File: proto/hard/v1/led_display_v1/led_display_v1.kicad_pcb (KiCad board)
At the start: 2 copper layers, 87 x 50 mm, 100 parts, among them U1 LCD_2.8_SPI, U2 74HCT595, U3 74HCT595, U4 74HCT595

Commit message: Generated gerbers for LED indicator.
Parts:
- moved REF** 0.76 mm to (109.4, 82.5)

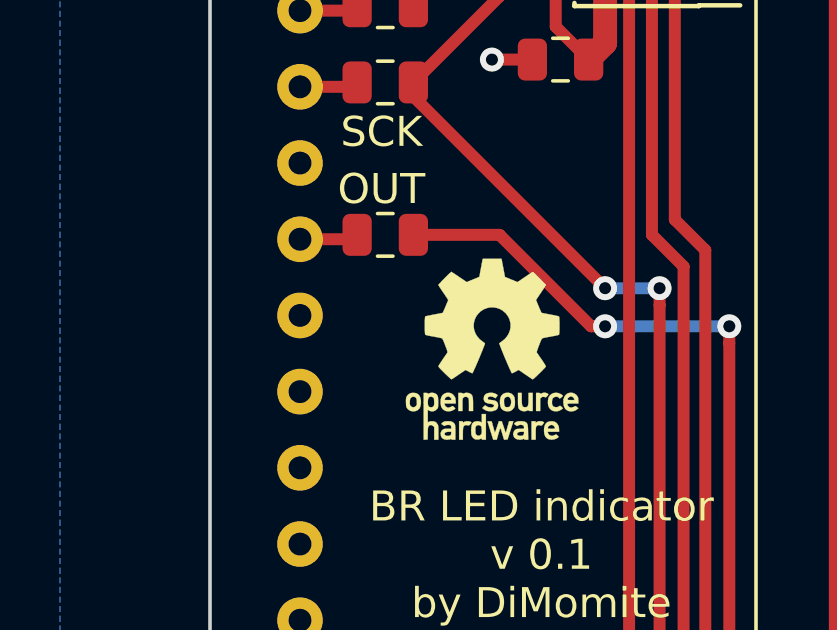
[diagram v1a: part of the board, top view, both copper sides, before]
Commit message: Added voltage divider to LED display data output. Module powered by +5V, so we may need divider to work with +3.3V components.
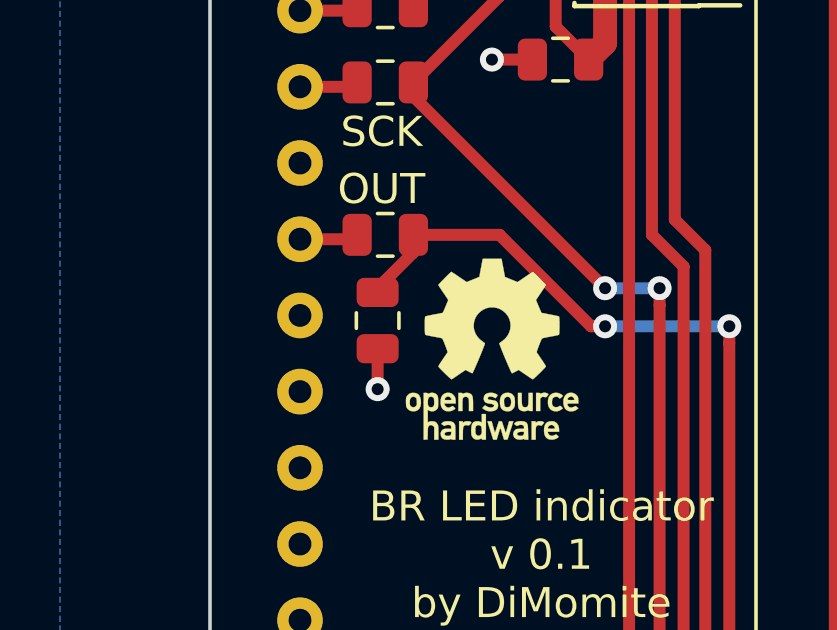
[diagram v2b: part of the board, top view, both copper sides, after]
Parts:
- added R38: 100R, Resistor_SMD:R_0805_2012Metric, F.Cu at (105.6, 81.5)
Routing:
- net /DataOut: track 64.1 -> 66.5 mm
- net GND: track 51.0 -> 52.3 mm, vias 38 -> 39

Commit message: Started implementation of LED display ctrl. Fixed wrong segments naming on led_display board.
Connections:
- R13 pad 2: /N2_E -> /N2_F
- R14 pad 2: /N2_F -> /N2_E
- R6 pad 2: /N1_E -> /N1_F
- R7 pad 2: /N1_F -> /N1_E
- U3 pad 6: /N1_F -> /N1_E
- U3 pad 7: /N1_E -> /N1_F
- U4 pad 6: /N2_F -> /N2_E
- U4 pad 7: /N2_E -> /N2_F

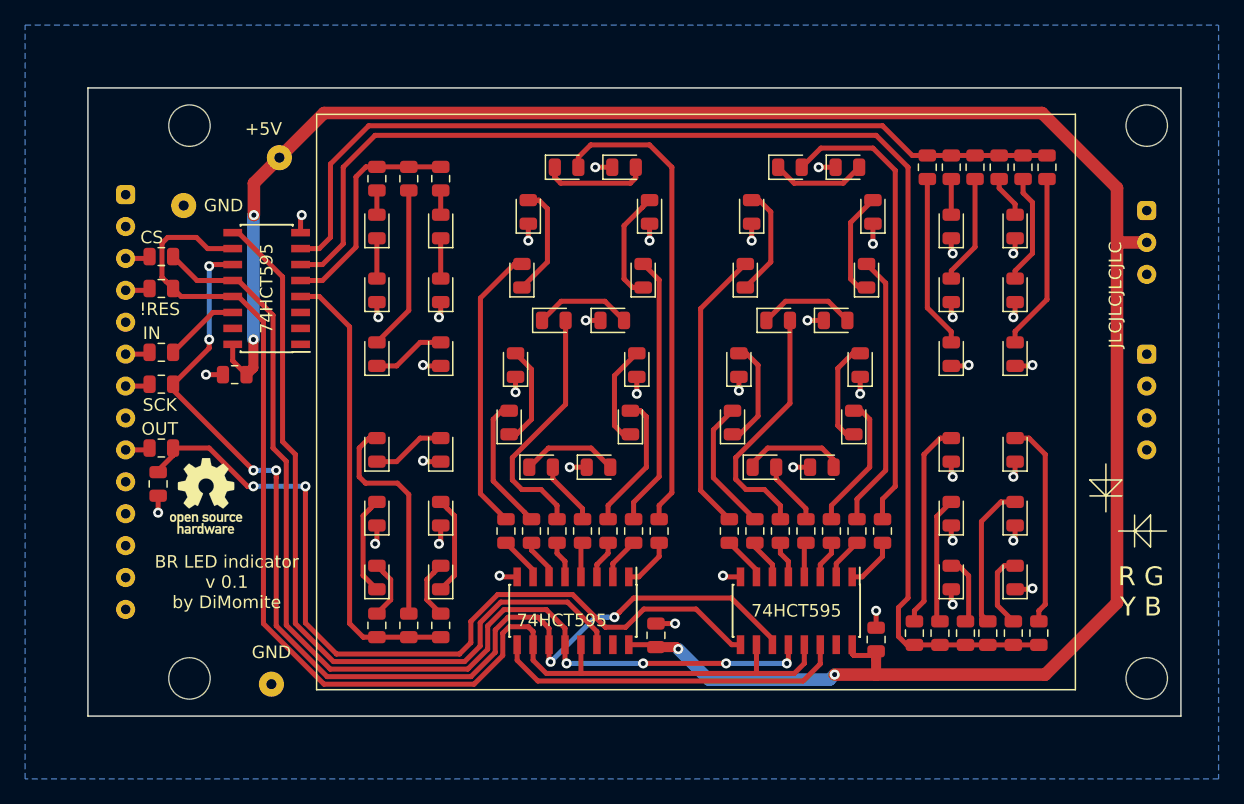
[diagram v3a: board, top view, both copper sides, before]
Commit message: Change SRCLR pin connection to external resistor pulled to +5. Board version increment to 0.2.
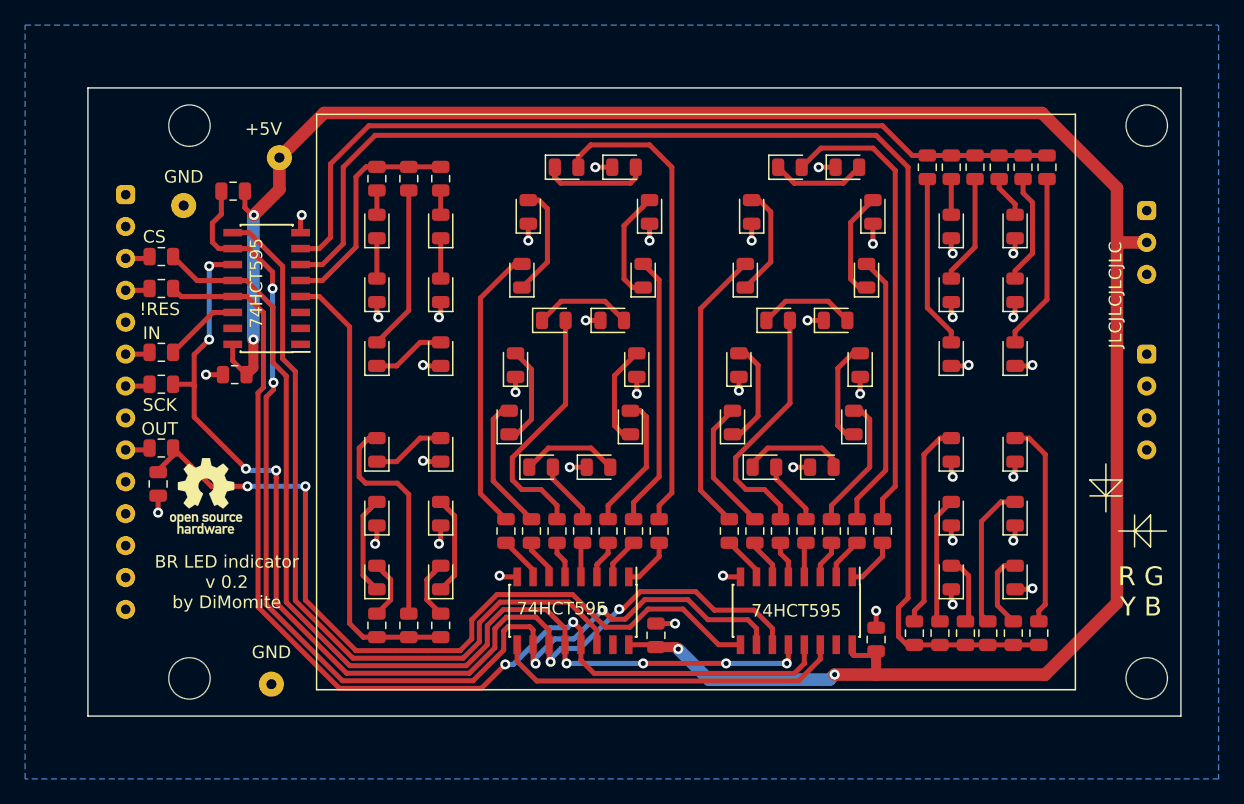
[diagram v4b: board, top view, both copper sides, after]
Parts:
- added R39: 10k, Resistor_SMD:R_0805_2012Metric, F.Cu at (111.6, 58.2)
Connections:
- U2 pad 10: /Reset -> /~SRCLR
- U3 pad 10: /Reset -> /~SRCLR
- U4 pad 10: /Reset -> /~SRCLR
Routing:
- net /~SRCLR: track 0.00 -> 89.0 mm, vias 0 -> 4
- net /Reset: track 99.8 -> 84.9 mm, vias 0 -> 2
- net +5V: track 174.5 -> 176.7 mm
- net /DataOut: track 66.5 -> 65.2 mm
- net /CS: track 84.2 -> 83.1 mm
- net Net-(U2-Pad9): track 63.8 -> 62.8 mm
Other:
- board text added: "BR LED indicator v 0.2 by DiMomite"
- board text removed: "BR LED indicator v 0.1 by DiMomite"
